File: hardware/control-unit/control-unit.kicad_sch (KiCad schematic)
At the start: 24 parts, among them Q1 AO3400A

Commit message: Updated USB data lines resistor and capacitor values
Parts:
- C7, C8: value ? -> TBD
- R7, R8: value ? -> 0
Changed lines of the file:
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@@
 			)
 		)
-		(property "Value" "?"
+		(property "Value" "TBD"
 			(at 190.5 72.3899 0)
 			(show_name no)
@@
 			)
 		)
-		(property "Value" "?"
+		(property "Value" "0"
 			(at 179.07 59.69 90)
 			(show_name no)
@@
 			)
 		)
-		(property "Value" "?"
+		(property "Value" "TBD"
 			(at 200.66 72.3899 0)
 			(show_name no)
@@
 			)
 		)
-		(property "Value" "?"
+		(property "Value" "0"
 			(at 179.0971 71.374 90)
 			(show_name no)

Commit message: Replaced control unit LDO with TPS7A02 on schematic
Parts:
- removed LDO1: AP7366EA-33W5-7, Package_TO_SOT_SMD:SOT-23-5_HandSoldering, symbol Custom_Symbols:AP7366EA-33W5-7
- added LDO1: TPS7A02xxxDBV, symbol Regulator_Linear:TPS7A02xxxDBV
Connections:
- net 3V3: now also LDO1.5 (OUT)
- net GND: now also LDO1.2 (GND)
- net V_{BAT}: now also LDO1.1 (IN)
- net at Q1.3 (D), R10.1: now also LDO1.3 (EN)

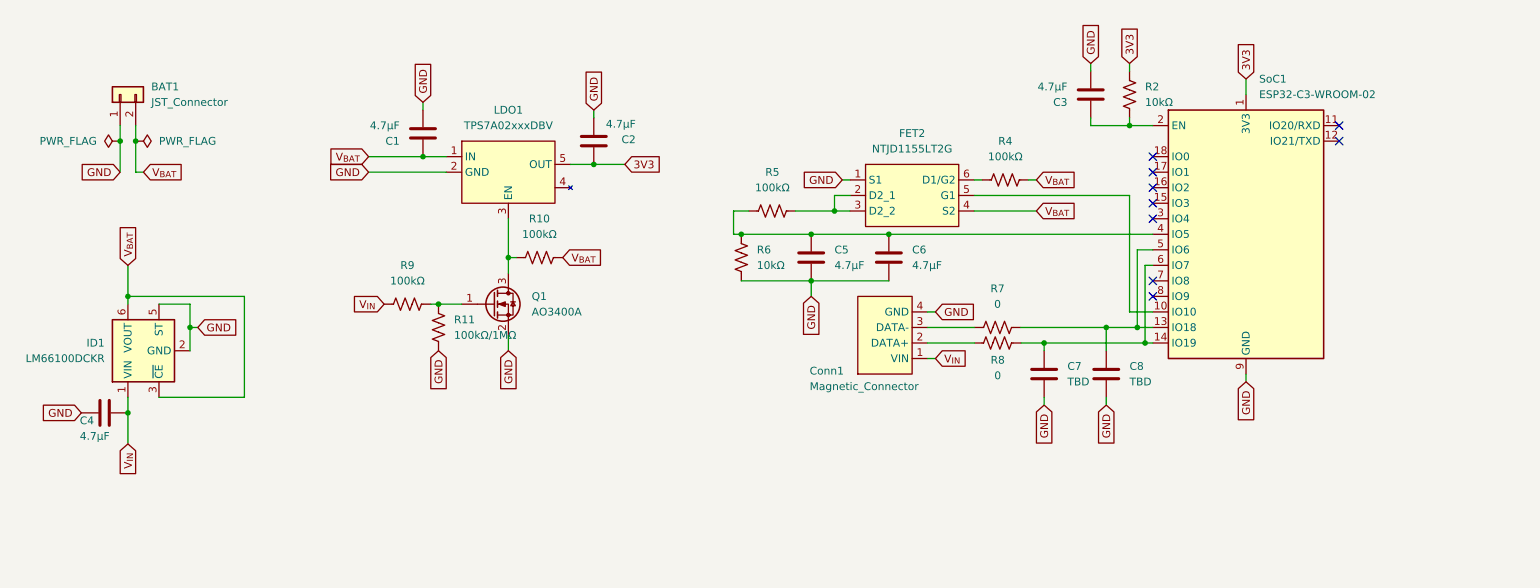
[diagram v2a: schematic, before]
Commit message: Remove outdated schematic review checklist and add new symbol files for AP7365. Minor improvements to schematic
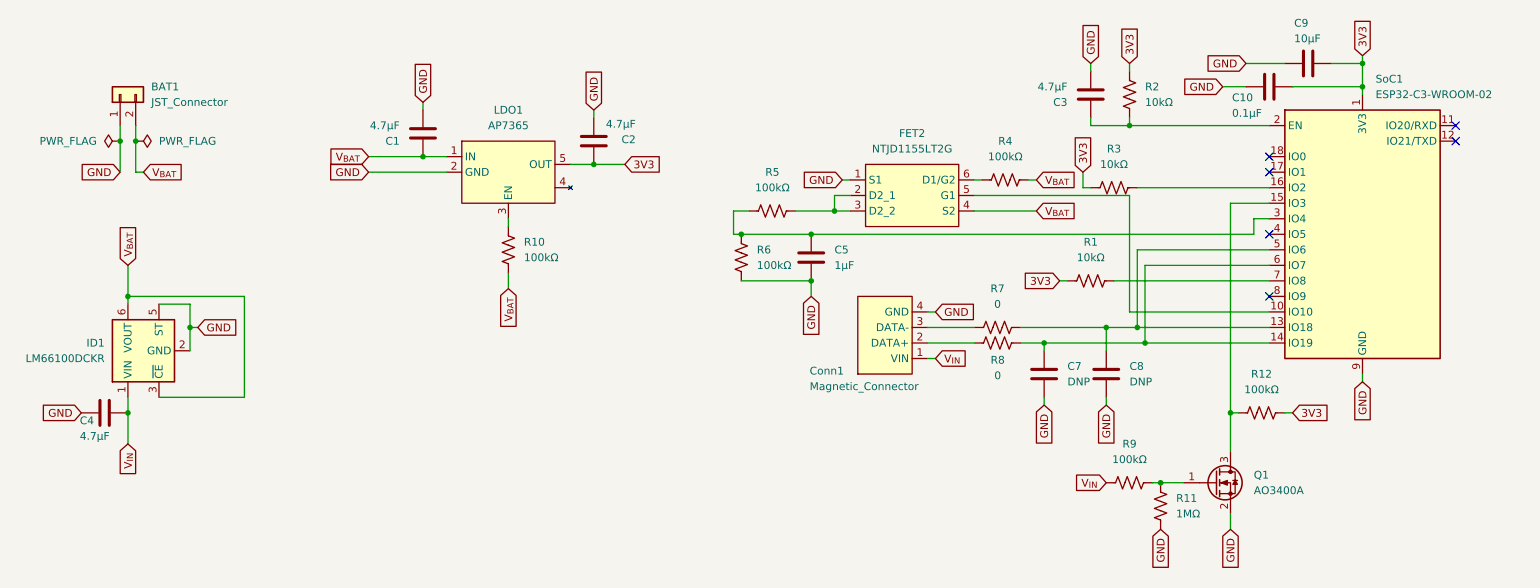
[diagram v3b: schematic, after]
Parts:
- removed C6: 4.7µF, Capacitor_SMD:C_0402_1005Metric_Pad0.74x0.62mm_HandSolder, symbol Device:C
- removed LDO1: TPS7A02xxxDBV, symbol Regulator_Linear:TPS7A02xxxDBV
- added C10: 0.1µF, Capacitor_SMD:C_0402_1005Metric_Pad0.74x0.62mm_HandSolder, symbol Device:C
- added C9: 10µF, Capacitor_SMD:C_0402_1005Metric_Pad0.74x0.62mm_HandSolder, symbol Device:C
- added LDO1: AP7365, symbol symbols:AP7365
- added R1, R3: 10kΩ, symbol Device:R_US
- added R12: 100kΩ, Resistor_SMD:R_0805_2012Metric_Pad1.20x1.40mm_HandSolder, symbol Device:R_US
- C5: value 4.7µF -> 1µF
- C7, C8: value TBD -> DNP
- R11: value 100kΩ/1MΩ -> 1MΩ
- R6: value 10kΩ -> 100kΩ
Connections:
- net 3V3: now also C10.2, C9.2, LDO1.5 (OUT), R1.1, R12.1, R3.1
- net GND: now also C10.1, C9.1, LDO1.2 (GND)
- net V_{BAT}: now also LDO1.1 (IN)
- net at Q1.3 (D): now also SoC1.15 (IO3), R12.2; no longer R10.1
- net at SoC1.16 (IO2): now also R3.2
- net at SoC1.3 (IO4): now also C5.2, R5.1, R6.2
- net at SoC1.7 (IO8): now also R1.2
- new net: LDO1.3 (EN), R10.1
- now unconnected: SoC1.4 (IO5)
- no-connect marks 9 -> 6
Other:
- moved on the sheet: Q1, R10, R11, R9, SoC1
